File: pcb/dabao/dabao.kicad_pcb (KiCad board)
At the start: 2 copper layers, 127.4 x 114.6 mm, 76 parts, among them J1 Conn_01x05, J2 USB_C_Receptacle_USB2.0_16P, J3 Conn_01x04, J4 MagConn_01x04_Pin, J5 Conn_Battery, J7 Conn_01x04, J8 Display, SW1 SW_RESET, SW2 SW_POWER, U1 nice_nano, U2 MCP23017_SP

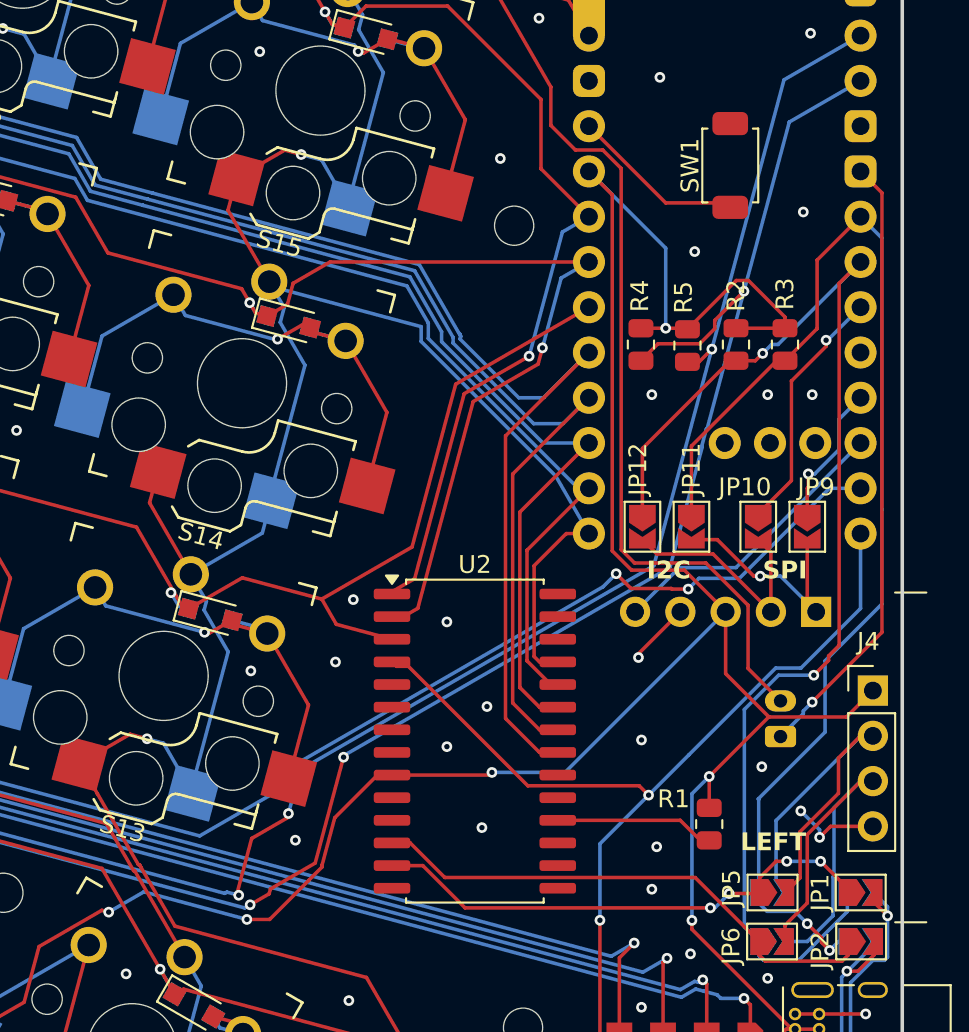
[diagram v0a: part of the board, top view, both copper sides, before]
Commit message: Touchpoint power MOSFET, decoupling cap for GPIO expander
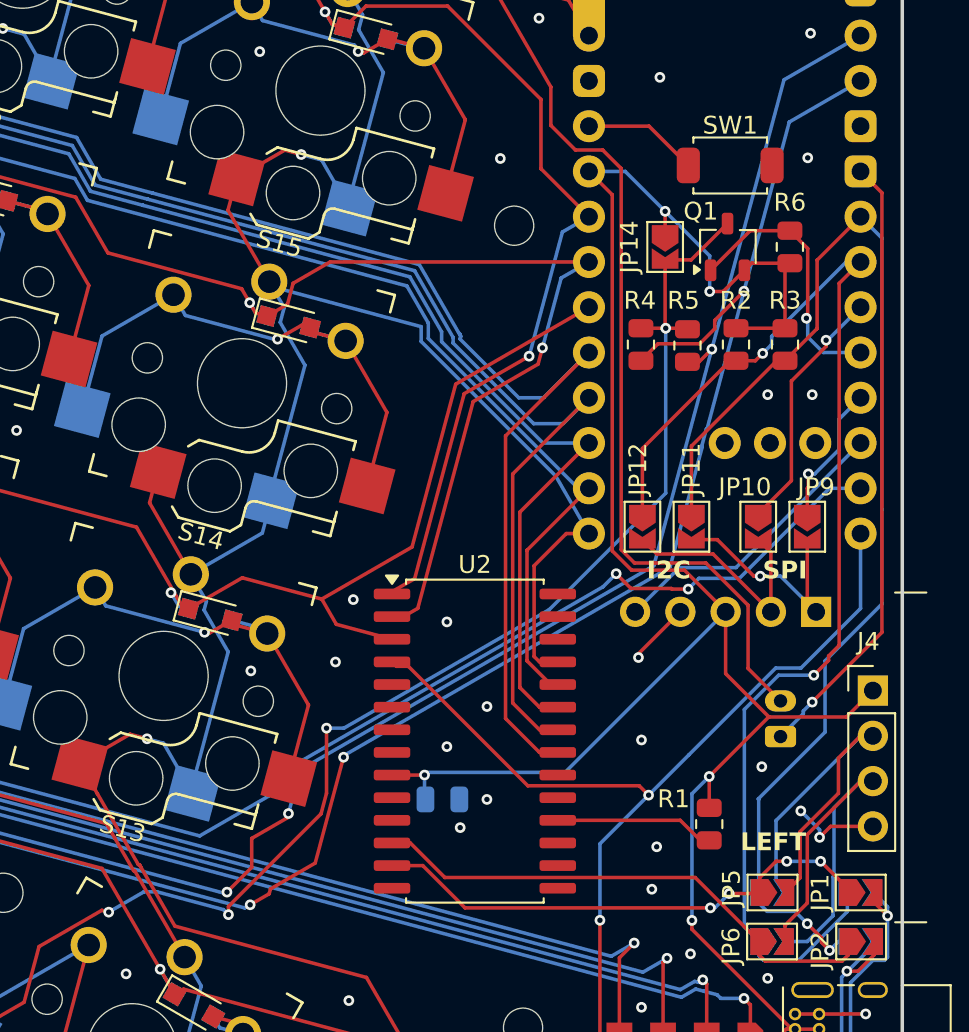
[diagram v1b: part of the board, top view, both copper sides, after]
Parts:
- added C2: 0.1uF, Capacitor_SMD:C_0805_2012Metric, B.Cu at (181.5, 105.5)
- added JP14: TP_ALWAYS_ON, Jumper:SolderJumper-2_P1.3mm_Open_TrianglePad1.0x1.5mm, F.Cu at (194.0, 74.5)
- added Q1: DMG2305UXQ, Library:DMG2305UXQ, F.Cu at (197.5, 74.5)
- added R6: 10k, Resistor_SMD:R_0805_2012Metric, F.Cu at (201.0, 74.5)
- turned SW1 to 0 degrees
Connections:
- C1 pad 1: VDD -> /TP_VDD
- J1 pad 5: VDD -> /TP_VDD
- R4 pad 2: VDD -> /TP_VDD
- R5 pad 2: VDD -> /TP_VDD
- U1 pad 8: unconnected-(U1-P0.24-Pad8) -> /TP_pwr_en
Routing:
- net /TP_VDD: track 0.00 -> 116.7 mm, vias 0 -> 6
- net VDD: track 195.0 -> 122.4 mm, vias 8 -> 5
- net /TP_pwr_en: track 0.00 -> 15.2 mm, vias 0 -> 1
- net /RESET: track 9.71 -> 6.49 mm
- net GND: vias 74 -> 72
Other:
- board text added: "jmklam v1.2"
- board text removed: "jmklam v1.1"

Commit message: Oops, not all the files were reflecting the R6 value change
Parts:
- R6: value 10k -> 470k
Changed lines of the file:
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@@
 			)
 		)
-		(property "Value" "10k"
+		(property "Value" "470k"
 			(at 0 1.65 90)
 			(layer "F.Fab")
